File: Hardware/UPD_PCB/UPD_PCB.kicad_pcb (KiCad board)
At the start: 6 copper layers, 142 parts, among them J1 25A Fuse holder, J10 Screw_Terminal_01x02, J11 Conn_01x02, J12 Conn_01x02, J2 Screw_Terminal_01x02, J3 Screw_Terminal_01x02, J4 Screw_Terminal_01x02, J5 Screw_Terminal_01x02, J6 Screw_Terminal_01x02, J7 Screw_Terminal_01x02, J8 Screw_Terminal_01x02, J9 Screw_Terminal_01x02, Q1 LMR51635XDDCR, Q2 LMR51635XDDCR, Q3 LMR51635XDDCR, Q4 LMR51635XDDCR, Q5 LMR51635XDDCR, Q6 LMR51635XDDCR, Q7 BSS84, U1 ACS711xEXLT-31AB, U2 INA219AxD, U3 INA219AxD, U4 INA219AxD, U5 INA219AxD, U6 INA219AxD, U7 INA219AxD

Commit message: First board layout
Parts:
- removed J9: Screw_Terminal_01x02, TerminalBlock_Philmore:TerminalBlock_Philmore_TB132_1x02_P5.00mm_Horizontal
- J10, J2: value Screw_Terminal_01x02 -> 796739-2; footprint TerminalBlock_Philmore:TerminalBlock_Philmore_TB132_1x02_P5.00mm_Horizontal -> Library:7967392
- J12: value Conn_01x02 -> Conn_01x01; footprint Connector_PinHeader_1.00mm:PinHeader_1x02_P1.00mm_Vertical -> Connector_PinHeader_1.00mm:PinHeader_1x01_P1.00mm_Vertical
- J3: value Screw_Terminal_01x02 -> Conn_01x02; footprint TerminalBlock_Philmore:TerminalBlock_Philmore_TB132_1x02_P5.00mm_Horizontal -> Connector_PinHeader_1.00mm:PinHeader_1x02_P1.00mm_Vertical
- J4, J5, J6, J7, J8: value Screw_Terminal_01x02 -> 1776119-2; footprint TerminalBlock_Philmore:TerminalBlock_Philmore_TB132_1x02_P5.00mm_Horizontal -> Library:17761192
- R13, R14, R26, R27, R36, R37: footprint Resistor_SMD:R_Shunt_Vishay_WSK2512_6332Metric_T2.21mm -> Library:R_shunt_different_pad_layout
- TP1, TP2, TP3, TP4, TP5, TP6, TP7, TP8, TP9: footprint TestPoint:TestPoint_Loop_D2.54mm_Drill1.5mm_Beaded -> TestPoint:TestPoint_THTPad_D1.0mm_Drill0.5mm
- moved R23 364.5 mm to (65.8, 95.1)
- moved D1 360.2 mm to (65.8, 93.1)
- moved R20 359.1 mm to (65.8, 91.1)
- moved J3 354.3 mm to (70.0, 114.0)
- moved J11 353.2 mm to (70.0, 110.0)
- moved R19 351.5 mm to (73.8, 93.1)
- moved Q7 351.5 mm to (69.8, 95.0)
- moved R24 347.6 mm to (81.4, 77.5), turned to 180 degrees
- moved U1 346.5 mm to (69.8, 90.1), turned to -90 degrees
- moved C31 343.1 mm to (73.8, 95.1), turned to 180 degrees
- moved C30 343.0 mm to (73.8, 91.1)
- moved R21 339.0 mm to (85.4, 77.5)
- moved R16 336.5 mm to (88.6, 84.1), turned to 90 degrees
- moved R15 336.4 mm to (88.6, 80.1), turned to -90 degrees
- moved C32 335.6 mm to (80.5, 84.5), turned to -90 degrees
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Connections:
- J4 pad 1: /Project Architecture/Schematics/connectors/+24V_out -> /Project Architecture/Schematics/connectors/+19V_out
- J5 pad 1: /Project Architecture/Schematics/connectors/+19V_out -> /Project Architecture/Schematics/connectors/+16V_out
- J6 pad 1: /Project Architecture/Schematics/connectors/+16V_out -> /Project Architecture/Schematics/connectors/+12V_1_out
- J7 pad 1: /Project Architecture/Schematics/connectors/+12V_1_out -> /Project Architecture/Schematics/connectors/+12V_2_out
- J8 pad 1: /Project Architecture/Schematics/connectors/+12V_2_out -> /Project Architecture/Schematics/connectors/+5V_out
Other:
- board outline added: 135 x 67.5 mm
- board text removed: "??? ??? ??? ??? ??? (slot) ??? ??? ??? ??? ???"
- board text removed: "???mm ???mm ???mm ???mm ???mm ???mm ???mm ???mm ???mm ???mm"
- board text removed: "Bottom Assembly (Scale 1:1)"
- board text removed: "Bottom Fabrication (Scale 1:1)"
- board text removed: "Bottom Test Points (Scale 1:1)"
- board text removed: "Bottom View"
- board text removed: "Count"
- board text removed: "Drill Drawing (Top View) (Scale 1:1)"
- board text removed: "FABRICATION NOTES (UNLESS OTHERWISE SPECIFIED) 1) OUTLINE DEFINED IN SEPARATE GERBER FILE WITH {dblquote}Edge_Cuts.GBR{dblquote} SUFFIX. DIMENSIONS OF CIRCUMSIZED RECTANGLE SHOWN ON THIS DWG FOR REF ONLY. 2) SEE SEPARATE DRILL FILES WITH {dblquote}.DRL{dblquote} SUFFIX FOR HOLE LOCATIONS. SELECTED HOLE LOCATIONS SHOWN ON THIS DWG FOR REF ONLY. 3) IMPEDANCE CONTROL REQUIRED. Microstrip 100-Ohm Dif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"
- board text removed: "Hole Size"
- board text removed: "Net"
- board text removed: "PCB3D_BR_BOARDNAME"
- board text removed: "PCB3D_TL_BOARDNAME"
- board text removed: "Plated"
- board text removed: "Plated Plated Plated Plated Plated Plated Plated Plated Plated Unplated"
- board text removed: "Ref."
- board text removed: "Symbol"
- board text removed: "TP? TP? TP?"
- board text removed: "Top Assembly (Scale 1:1)"
- board text removed: "Top Fabrication (Scale 1:1)"
- board text removed: "Top Test Points (Scale 1:1)"
- board text removed: "Top View"
- board text removed: "X"
- board text removed: "X [mm]"
- board text removed: "Y"
- board text removed: "Y [mm]"

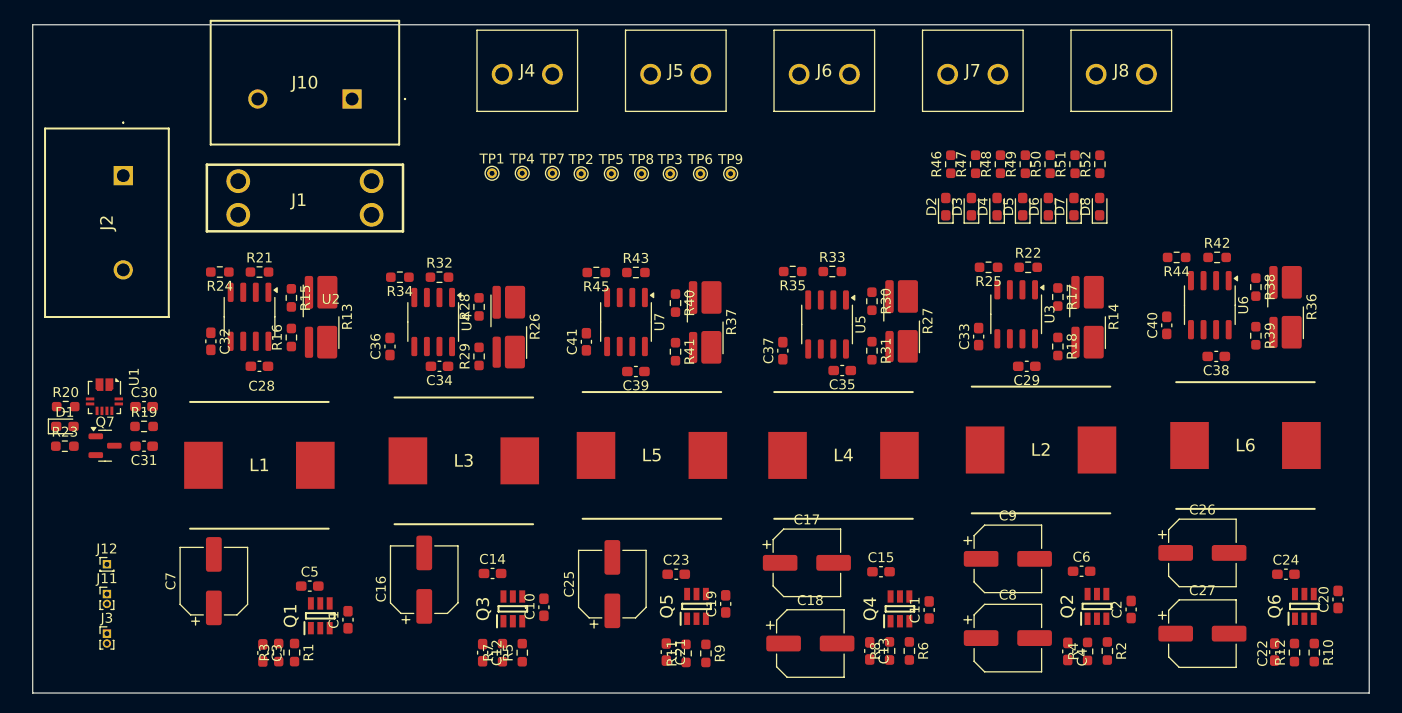
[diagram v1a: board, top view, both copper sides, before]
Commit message: Pcb layout before changing inductor
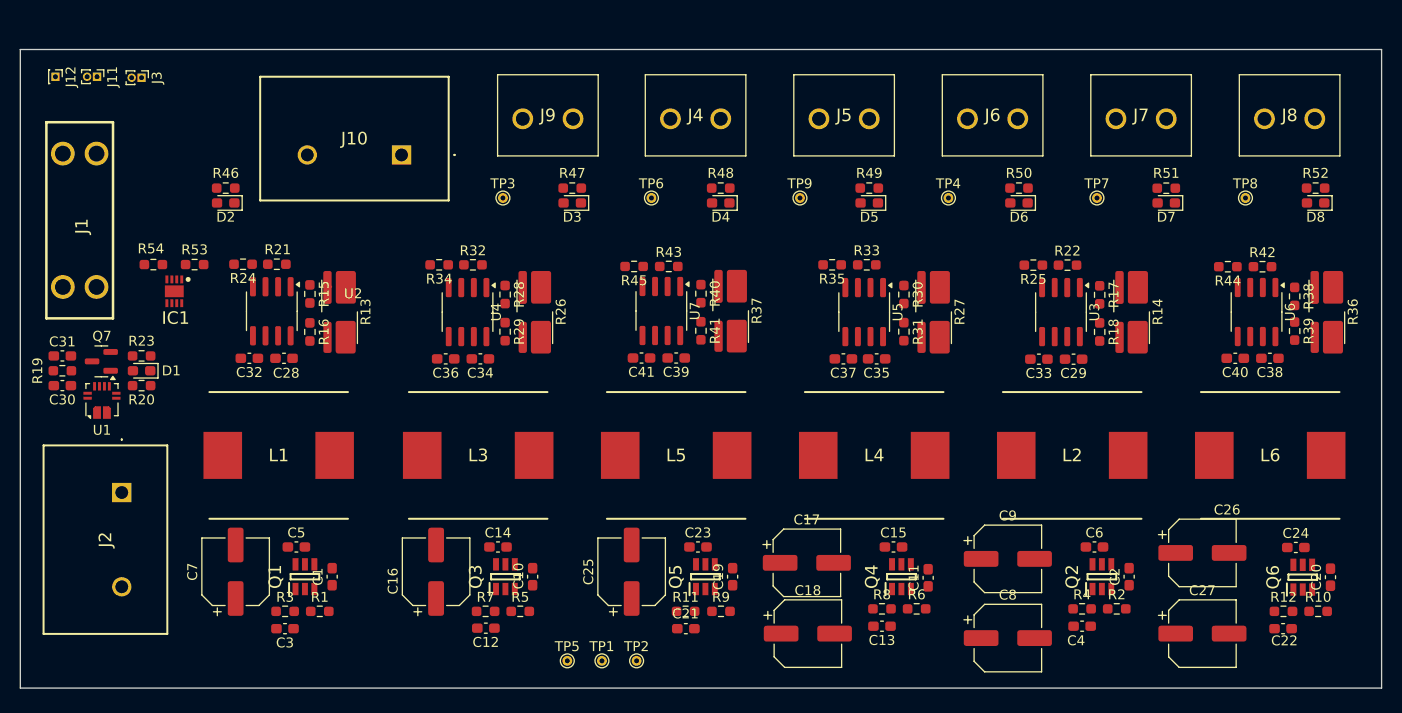
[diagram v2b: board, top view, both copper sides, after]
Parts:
- added IC1: STS30-DIS, Library:SON50P250X250X100-9N-D, F.Cu at (76.8, 79.4)
- added J9: 1776119-2, Library:17761192, F.Cu at (117.1, 62.0)
- added R53: 10k, Resistor_SMD:R_0603_1608Metric_Pad0.98x0.95mm_HandSolder, F.Cu at (78.9, 76.7)
- added R54: 10k, Resistor_SMD:R_0603_1608Metric_Pad0.98x0.95mm_HandSolder, F.Cu at (74.7, 76.7)
- moved R46 73.3 mm to (82.0, 69.0), turned to 180 degrees
- moved D2 72.7 mm to (82.0, 70.5), turned to 180 degrees
- moved TP8 61.0 mm to (185.0, 70.0)
- moved J3 56.3 mm to (73.5, 57.9), turned to -90 degrees
- moved TP7 55.1 mm to (170.0, 70.0)
- moved J11 52.3 mm to (69.0, 57.8), turned to -90 degrees
- moved TP1 50.5 mm to (120.0, 116.8)
- moved J12 49.5 mm to (64.8, 57.8), turned to -90 degrees
- moved TP2 49.5 mm to (123.5, 116.8)
- moved TP5 49.4 mm to (116.5, 116.8)
- moved TP4 43.1 mm to (155.0, 70.0)
- moved R47 40.8 mm to (117.0, 69.0), turned to 180 degrees
- moved D3 40.3 mm to (117.0, 70.5), turned to 180 degrees
- moved J2 32.0 mm to (71.5, 99.8)
- moved R48 28.4 mm to (132.0, 69.0), turned to 180 degrees
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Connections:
- C1 pad 1: /Project Architecture/Schematics/power_distrubution/+42V -> +42V
- C10 pad 1: /Project Architecture/Schematics/power_distrubution/+42V -> +42V
- C11 pad 1: /Project Architecture/Schematics/power_distrubution/+42V -> +42V
- C12 pad 2: /Project Architecture/Schematics/power_distrubution/+19V -> +19V
- C13 pad 2: /Project Architecture/Schematics/power_distrubution/+12V_2 -> +12V_2
- C16 pad 2: /Project Architecture/Schematics/power_distrubution/+19V -> +19V
- C17 pad 2: /Project Architecture/Schematics/power_distrubution/+12V_2 -> +12V_2
- C18 pad 2: /Project Architecture/Schematics/power_distrubution/+12V_2 -> +12V_2
- C19 pad 1: /Project Architecture/Schematics/power_distrubution/+42V -> +42V
- C2 pad 1: /Project Architecture/Schematics/power_distrubution/+42V -> +42V
- C20 pad 1: /Project Architecture/Schematics/power_distrubution/+42V -> +42V
- C21 pad 2: /Project Architecture/Schematics/power_distrubution/+16V -> +16V
- C22 pad 2: /Project Architecture/Schematics/power_distrubution/+5V_NS -> +5V_NS
- C25 pad 2: /Project Architecture/Schematics/power_distrubution/+16V -> +16V
- C26 pad 2: /Project Architecture/Schematics/power_distrubution/+5V_NS -> +5V_NS
- C27 pad 2: /Project Architecture/Schematics/power_distrubution/+5V_NS -> +5V_NS
- C3 pad 2: /Project Architecture/Schematics/power_distrubution/+24V -> +24V
- C31 pad 1: /Project Architecture/Schematics/current_sensing/VIOUT -> VIOUT
- C4 pad 2: /Project Architecture/Schematics/power_distrubution/+12V_1 -> +12V_1
- C7 pad 2: /Project Architecture/Schematics/power_distrubution/+24V -> +24V
- C8 pad 2: /Project Architecture/Schematics/power_distrubution/+12V_1 -> +12V_1
- C9 pad 2: /Project Architecture/Schematics/power_distrubution/+12V_1 -> +12V_1
- D2 pad 2: /Project Architecture/Schematics/connectors/+MD_42V -> +42V
- D3 pad 2: /Project Architecture/Schematics/connectors/+24V_out -> +24V_out
- D4 pad 2: /Project Architecture/Schematics/connectors/+19V_out -> +19V_out
- D5 pad 2: /Project Architecture/Schematics/connectors/+16V_out -> +16V_out
- D6 pad 2: /Project Architecture/Schematics/connectors/+12V_1_out -> +12V_1_out
- D7 pad 2: /Project Architecture/Schematics/connectors/+12V_2_out -> +12V_2_out
- D8 pad 2: /Project Architecture/Schematics/connectors/+5V_out -> +5V_out
- J1 pad 1: /Project Architecture/Schematics/connectors/+42V -> +42V
- J1 pad 3: /Project Architecture/Schematics/connectors/+42V -> +42V
- J10 pad 1: Net-(J1-Pad2) -> GND
- J10 pad 2: GND -> Net-(J1-Pad2)
- J11 pad 1: /Project Architecture/Schematics/connectors/INA_SDA -> INA_SDA
- J11 pad 2: /Project Architecture/Schematics/connectors/INA_SCL -> INA_SCL
- J12 pad 1: /Project Architecture/Schematics/connectors/VIOUT -> VIOUT
- J2 pad 1: GND -> IP+
- J2 pad 2: /Project Architecture/Schematics/connectors/IP+ -> GND
- J4 pad 1: /Project Architecture/Schematics/connectors/+19V_out -> +19V_out
- J5 pad 1: /Project Architecture/Schematics/connectors/+16V_out -> +16V_out
- J6 pad 1: /Project Architecture/Schematics/connectors/+12V_1_out -> +12V_1_out
- J7 pad 1: /Project Architecture/Schematics/connectors/+12V_2_out -> +12V_2_out
- J8 pad 1: /Project Architecture/Schematics/connectors/+5V_out -> +5V_out
- L1 pad 2: /Project Architecture/Schematics/power_distrubution/+24V -> +24V
- L2 pad 2: /Project Architecture/Schematics/power_distrubution/+12V_1 -> +12V_1
- L3 pad 2: /Project Architecture/Schematics/power_distrubution/+19V -> +19V
- L4 pad 2: /Project Architecture/Schematics/power_distrubution/+12V_2 -> +12V_2
- L5 pad 2: /Project Architecture/Schematics/power_distrubution/+16V -> +16V
- L6 pad 2: /Project Architecture/Schematics/power_distrubution/+5V_NS -> +5V_NS
- Q1 pad 2: /Project Architecture/Schematics/power_distrubution/+42V -> +42V
- Q1 pad 3: /Project Architecture/Schematics/power_distrubution/+42V -> +42V
- Q2 pad 2: /Project Architecture/Schematics/power_distrubution/+42V -> +42V
- Q2 pad 3: /Project Architecture/Schematics/power_distrubution/+42V -> +42V
- Q3 pad 2: /Project Architecture/Schematics/power_distrubution/+42V -> +42V
- Q3 pad 3: /Project Architecture/Schematics/power_distrubution/+42V -> +42V
- Q4 pad 2: /Project Architecture/Schematics/power_distrubution/+42V -> +42V
- Q4 pad 3: /Project Architecture/Schematics/power_distrubution/+42V -> +42V
- Q5 pad 2: /Project Architecture/Schematics/power_distrubution/+42V -> +42V
- Q5 pad 3: /Project Architecture/Schematics/power_distrubution/+42V -> +42V
- Q6 pad 2: /Project Architecture/Schematics/power_distrubution/+42V -> +42V
- Q6 pad 3: /Project Architecture/Schematics/power_distrubution/+42V -> +42V
- R11 pad 1: /Project Architecture/Schematics/power_distrubution/+16V -> +16V
- R12 pad 1: /Project Architecture/Schematics/power_distrubution/+5V_NS -> +5V_NS
- R13 pad 1: /Project Architecture/Schematics/current_sensing/+24V -> +24V
- R14 pad 1: /Project Architecture/Schematics/current_sensing/+12V_1 -> +12V_1
- R19 pad 2: /Project Architecture/Schematics/current_sensing/VIOUT -> VIOUT
- R21 pad 1: /Project Architecture/Schematics/current_sensing/INA_SDA -> INA_SDA
- R22 pad 1: /Project Architecture/Schematics/current_sensing/INA_SDA -> INA_SDA
- R24 pad 1: /Project Architecture/Schematics/current_sensing/INA_SCL -> INA_SCL
- R25 pad 1: /Project Architecture/Schematics/current_sensing/INA_SCL -> INA_SCL
- R26 pad 1: /Project Architecture/Schematics/current_sensing/+19V -> +19V
- R27 pad 1: /Project Architecture/Schematics/current_sensing/+12V_2 -> +12V_2
- R3 pad 1: /Project Architecture/Schematics/power_distrubution/+24V -> +24V
- R32 pad 1: /Project Architecture/Schematics/current_sensing/INA_SDA -> INA_SDA
- R33 pad 1: /Project Architecture/Schematics/current_sensing/INA_SDA -> INA_SDA
- R34 pad 1: /Project Architecture/Schematics/current_sensing/INA_SCL -> INA_SCL
- R35 pad 1: /Project Architecture/Schematics/current_sensing/INA_SCL -> INA_SCL
- R36 pad 1: /Project Architecture/Schematics/current_sensing/+5V_NS -> +5V_NS
- R36 pad 4: +5V -> +5V_out
- R37 pad 1: /Project Architecture/Schematics/current_sensing/+16V -> +16V
- R4 pad 1: /Project Architecture/Schematics/power_distrubution/+12V_1 -> +12V_1
- R42 pad 1: /Project Architecture/Schematics/current_sensing/INA_SDA -> INA_SDA
- R43 pad 1: /Project Architecture/Schematics/current_sensing/INA_SDA -> INA_SDA
- R44 pad 1: /Project Architecture/Schematics/current_sensing/INA_SCL -> INA_SCL
- R45 pad 1: /Project Architecture/Schematics/current_sensing/INA_SCL -> INA_SCL
- R7 pad 1: /Project Architecture/Schematics/power_distrubution/+19V -> +19V
- R8 pad 1: /Project Architecture/Schematics/power_distrubution/+12V_2 -> +12V_2
- TP3 pad 1: /Project Architecture/Schematics/current_sensing/+24V -> +24V
- TP4 pad 1: /Project Architecture/Schematics/current_sensing/+12V_1 -> +12V_1
- TP6 pad 1: /Project Architecture/Schematics/current_sensing/+19V -> +19V
- TP7 pad 1: /Project Architecture/Schematics/current_sensing/+12V_2 -> +12V_2
- TP8 pad 1: /Project Architecture/Schematics/current_sensing/+5V_NS -> +5V_NS
- TP9 pad 1: /Project Architecture/Schematics/current_sensing/+16V -> +16V
- U1 pad 1: /Project Architecture/Schematics/current_sensing/IP+ -> IP+
- U1 pad 2: /Project Architecture/Schematics/current_sensing/+42V -> +42V
- U2 pad 3: /Project Architecture/Schematics/current_sensing/INA_SDA -> INA_SDA
- U2 pad 4: /Project Architecture/Schematics/current_sensing/INA_SCL -> INA_SCL
- U3 pad 3: /Project Architecture/Schematics/current_sensing/INA_SDA -> INA_SDA
- U3 pad 4: /Project Architecture/Schematics/current_sensing/INA_SCL -> INA_SCL
- U4 pad 3: /Project Architecture/Schematics/current_sensing/INA_SDA -> INA_SDA
- U4 pad 4: /Project Architecture/Schematics/current_sensing/INA_SCL -> INA_SCL
- U5 pad 1: /Project Architecture/Schematics/current_sensing/INA_SCL -> INA_SCL
- U5 pad 2: /Project Architecture/Schematics/current_sensing/INA_SCL -> INA_SCL
- U5 pad 3: /Project Architecture/Schematics/current_sensing/INA_SDA -> INA_SDA
- U5 pad 4: /Project Architecture/Schematics/current_sensing/INA_SCL -> INA_SCL
- U6 pad 3: /Project Architecture/Schematics/current_sensing/INA_SDA -> INA_SDA
- U6 pad 4: /Project Architecture/Schematics/current_sensing/INA_SCL -> INA_SCL
- U7 pad 1: /Project Architecture/Schematics/current_sensing/INA_SDA -> INA_SDA
- U7 pad 2: /Project Architecture/Schematics/current_sensing/INA_SDA -> INA_SDA
- U7 pad 3: /Project Architecture/Schematics/current_sensing/INA_SDA -> INA_SDA
- U7 pad 4: /Project Architecture/Schematics/current_sensing/INA_SCL -> INA_SCL
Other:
- board size 135 x 67.5 mm -> 137.5 x 64.5 mm

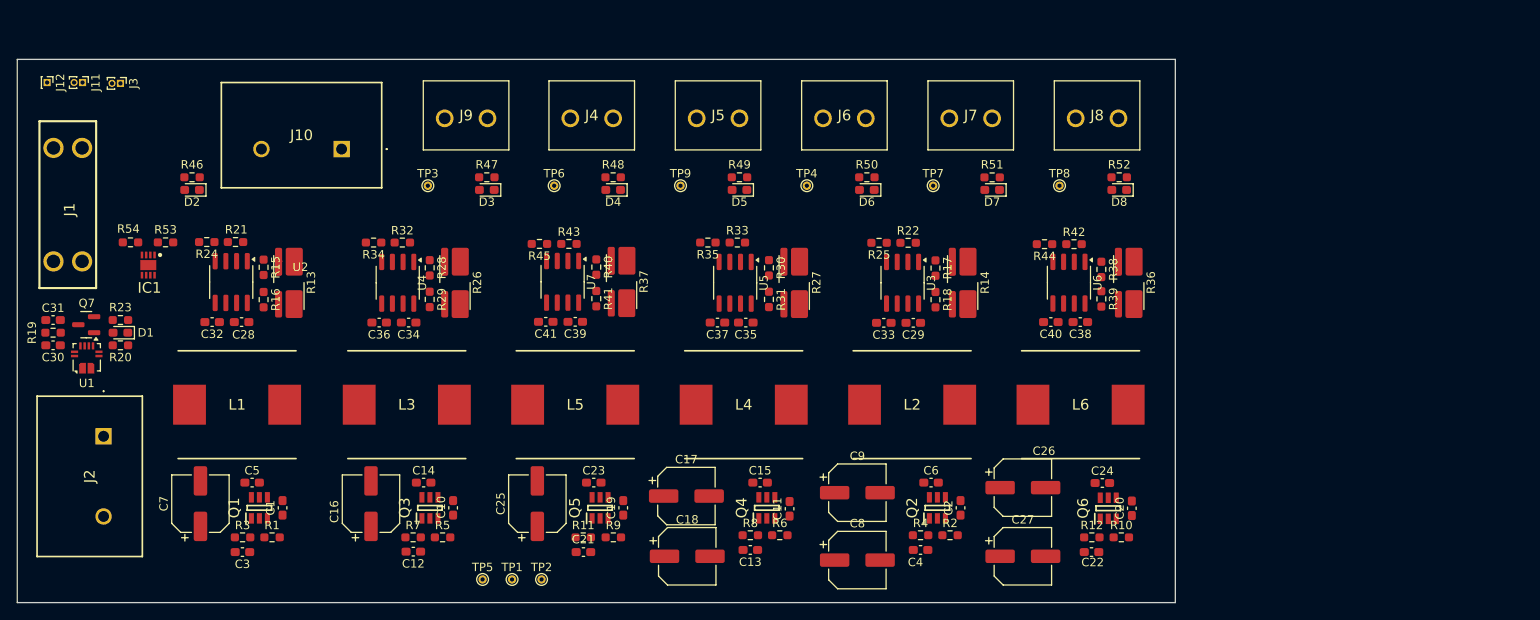
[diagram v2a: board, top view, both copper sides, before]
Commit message: Routed main traces
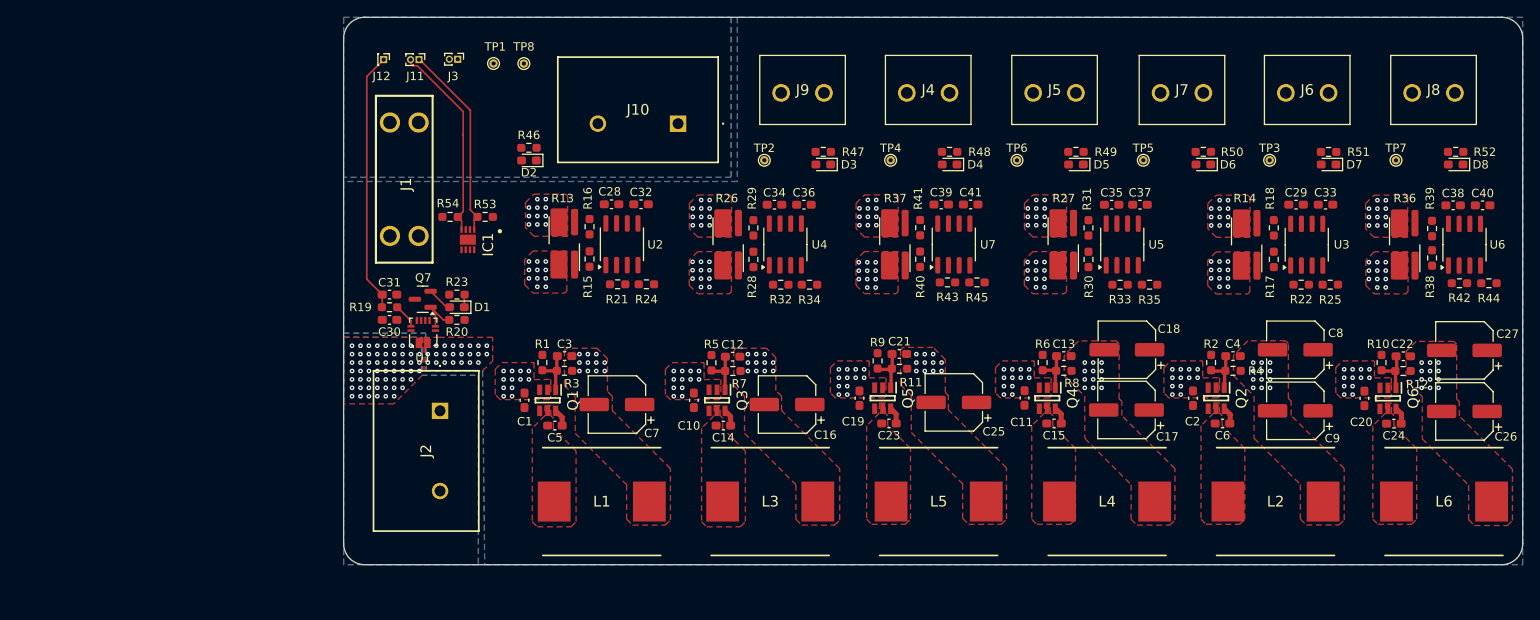
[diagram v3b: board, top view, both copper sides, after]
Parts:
- removed TP9: TestPoint, TestPoint:TestPoint_THTPad_D1.0mm_Drill0.5mm
- moved TP3 100.0 mm to (209.9, 67.0)
- moved TP5 92.9 mm to (194.9, 67.0)
- moved TP8 65.2 mm to (121.4, 55.5)
- moved TP1 61.3 mm to (117.8, 55.5)
- moved C27 57.8 mm to (233.1, 89.5), turned to 180 degrees
- moved C8 57.7 mm to (213.0, 89.5), turned to 180 degrees
- moved C18 57.7 mm to (193.0, 89.5), turned to 180 degrees
- moved TP2 56.4 mm to (149.9, 67.0)
- moved J6 55.0 mm to (216.9, 59.0)
- moved TP6 55.0 mm to (179.9, 67.0)
- moved TP7 55.0 mm to (224.9, 67.0)
- moved C33 54.3 mm to (216.6, 72.2), turned to 0 degrees
- moved R25 53.8 mm to (217.1, 81.8), turned to 0 degrees
- moved C17 53.2 mm to (192.9, 96.6), turned to 180 degrees
- moved C26 53.2 mm to (233.1, 96.8), turned to 180 degrees
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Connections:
- C30 pad 1: +5V -> +5V_out
- C32 pad 2: +5V -> +5V_out
- C33 pad 2: +5V -> +5V_out
- C36 pad 2: +5V -> +5V_out
- C37 pad 2: +5V -> +5V_out
- C40 pad 2: +5V -> +5V_out
- C41 pad 2: +5V -> +5V_out
- IC1 pad 5: +5V -> +5V_out
- J3 pad 2: +5V -> +5V_out
- Q7 pad 3: +5V -> +5V_out
- R20 pad 1: +5V -> +5V_out
- R21 pad 2: +5V -> +5V_out
- R22 pad 2: +5V -> +5V_out
- R24 pad 2: +5V -> +5V_out
- R25 pad 2: +5V -> +5V_out
- R32 pad 2: +5V -> +5V_out
- R33 pad 2: +5V -> +5V_out
- R34 pad 2: +5V -> +5V_out
- R35 pad 2: +5V -> +5V_out
- R42 pad 2: +5V -> +5V_out
- R43 pad 2: +5V -> +5V_out
- R44 pad 2: +5V -> +5V_out
- R45 pad 2: +5V -> +5V_out
- R53 pad 2: +5V -> +5V_out
- R54 pad 2: +5V -> +5V_out
- TP2 pad 1: GND -> +24V_out
- TP3 pad 1: +24V -> +12V_1_out
- TP4 pad 1: +12V_1 -> +19V_out
- TP5 pad 1: GND -> +12V_2_out
- TP6 pad 1: +19V -> +16V_out
- TP7 pad 1: +12V_2 -> +5V_out
- TP8 pad 1: +5V_NS -> Net-(J1-Pad2)
- U1 pad 10: +5V -> +5V_out
- U2 pad 5: +5V -> +5V_out
- U3 pad 1: +5V -> +5V_out
- U3 pad 5: +5V -> +5V_out
- U4 pad 2: +5V -> +5V_out
- U4 pad 5: +5V -> +5V_out
- U5 pad 5: +5V -> +5V_out
- U6 pad 1: +5V -> +5V_out
- U6 pad 2: +5V -> +5V_out
- U6 pad 5: +5V -> +5V_out
- U7 pad 5: +5V -> +5V_out
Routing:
- net VIOUT: track 0.00 -> 31.0 mm
- net INA_SCL: track 0.00 -> 23.6 mm
- net INA_SDA: track 0.00 -> 23.3 mm
- net Net-(Q1-FB): track 0.00 -> 5.82 mm
- net Net-(Q3-FB): track 0.00 -> 5.57 mm
- net Net-(Q2-FB): track 0.00 -> 5.44 mm
- net Net-(Q6-FB): track 0.00 -> 5.44 mm
- net Net-(Q5-FB): track 0.00 -> 5.44 mm
- net Net-(Q4-FB): track 0.00 -> 5.44 mm
- net Net-(Q7-G): track 0.00 -> 5.34 mm
- net Net-(D1-A): track 0.00 -> 3.04 mm
- net Net-(U1-VIOUT): track 0.00 -> 2.96 mm
- net Net-(Q1-CB): track 0.00 -> 2.07 mm
- net Net-(Q6-CB): track 0.00 -> 2.02 mm
- net Net-(Q5-CB): track 0.00 -> 2.02 mm
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- added copper zone on F.Cu, net +12V_1
- added copper zone on In3.Cu, net +12V_1
- added copper zone on F.Cu, net +12V_1_out
- added copper zone on In3.Cu, net +12V_1_out
- added copper zone on F.Cu, net +12V_2
- added copper zone on In3.Cu, net +12V_2
- added copper zone on F.Cu, net +12V_2_out
- added copper zone on In3.Cu, net +12V_2_out
- added copper zone on F.Cu, net +16V
- added copper zone on In3.Cu, net +16V
- added copper zone on F.Cu, net +16V_out
- added copper zone on In3.Cu, net +16V_out
- added copper zone on F.Cu, net +19V
- added copper zone on In3.Cu, net +19V
- added copper zone on F.Cu, net +19V_out
- added copper zone on F.Cu, net +24V
- added copper zone on In3.Cu, net +24V
- added copper zone on F.Cu, net +24V_out
- added copper zone on In3.Cu, net +24V_out
- added copper zone on B.Cu, net +42V
- added copper zone on F.Cu, net +42V
- added copper zone on F.Cu, net +5V_NS
- added copper zone on In3.Cu, net +5V_NS
- added copper zone on F.Cu, net +5V_out
- added copper zone on In3.Cu, net +5V_out
- added copper zone on In1.Cu, net GND
- added copper zone on In4.Cu, net GND
- added copper zone on B.Cu, net IP+
- added copper zone on F.Cu, net IP+
- added copper zone on B.Cu, net Net-(J1-Pad2)
- added copper zone on F.Cu, net Net-(Q1-SW)
- added copper zone on F.Cu, net Net-(Q2-SW)
- added copper zone on F.Cu, net Net-(Q3-SW)
- added copper zone on F.Cu, net Net-(Q4-SW)
- added copper zone on F.Cu, net Net-(Q5-SW)
- added copper zone on F.Cu, net Net-(Q6-SW)
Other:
- board size 137.5 x 64.5 mm -> 140 x 65 mm
